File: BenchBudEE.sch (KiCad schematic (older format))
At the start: 0 parts

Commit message: Module 2, Unit 13 Defining Your Inputs and Outputs
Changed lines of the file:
@@
 $EndDescr
 $Sheet
-S 3200 5700 2200 1350
+S 2100 3450 1850 3650
 U 52EBE680
 F0 "Arduino" 50
 F1 "Arduino.sch" 50
+F2 "Relay+" O R 3950 6350 60
+F3 "Relay-" I R 3950 6550 60
+F4 "MOSI" O R 3950 5550 60
+F5 "MISO" I R 3950 5700 60
+F6 "SCLK" O R 3950 5850 60
+F7 "CS_N" O R 3950 6000 60
+F8 "LED_EN" O R 3950 4850 60
+F9 "LED_FREQ" O R 3950 5050 60
+F10 "FAN_EN" O R 3950 4300 60
+F11 "TACH_MEAS" I R 3950 4450 60
 $EndSheet
 $Sheet
@@
 F0 "Relay" 50
 F1 "Relay.sch" 50
+F2 "DIN+" I L 7600 6000 60
+F3 "DIN-" I L 7600 6250 60
+F4 "Relay+" I R 9450 6000 60
+F5 "Relay-" I R 9450 6200 60
 $EndSheet
 $Sheet
-S 3200 1350 1800 1150
+S 2050 1150 1800 1150
 U 52EBE800
 F0 "Power" 50
@@
 F0 "LED_Driver" 50
 F1 "LED_Driver.sch" 50
-$EndSheet
-$Sheet
-S 7550 1000 1850 1150
-U 52EBE84E
-F0 "Fan" 50
-F1 "Fan.sch" 50
+F2 "En" I L 7550 2800 60
+F3 "FREQ" I L 7550 3000 60
+F4 "String+" I R 9400 2800 60
+F5 "String-" O R 9400 3000 60
 $EndSheet
 $Sheet
@@
 F2 "TC IN +" I R 9450 4250 60
 F3 "TC IN -" I R 9450 4500 60
+F4 "MOSI" I L 7600 4250 60
+F5 "MISO" O L 7600 4400 60
+F6 "SCLK" I L 7600 4550 60
+F7 "CS_N" I L 7600 4700 60
+$EndSheet
+$Sheet
+S 7550 1000 1850 1150
+U 52EBE84E
+F0 "Fan" 50
+F1 "Fan.sch" 50
+F2 "Power+" O R 9400 1200 60
+F3 "Power-" I R 9400 1400 60
+F4 "Tach" I R 9400 1600 60
+F5 "Tack_Out" O L 7550 1600 60
+F6 "Fan_In" I L 7550 1200 60
 $EndSheet
 $EndSCHEMATC

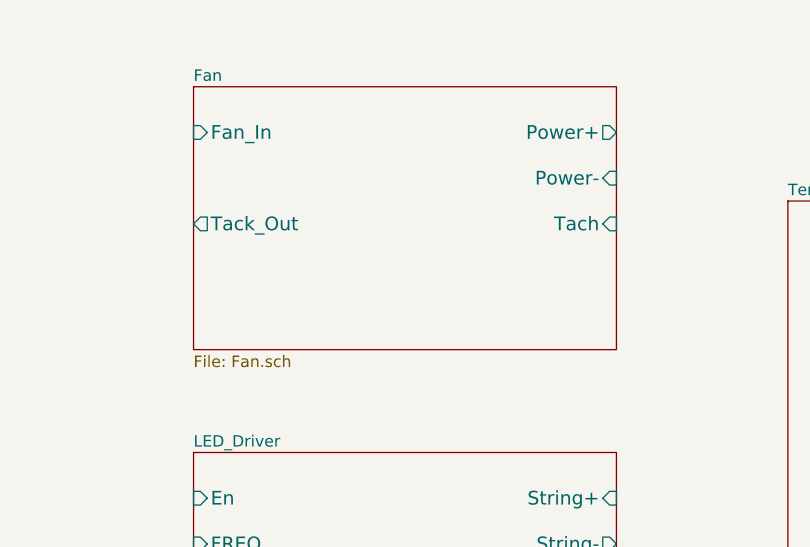
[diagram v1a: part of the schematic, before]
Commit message: 3.4 Understanding The Current/Fan Driver Module Added circuit to the Current/Fan Driver module
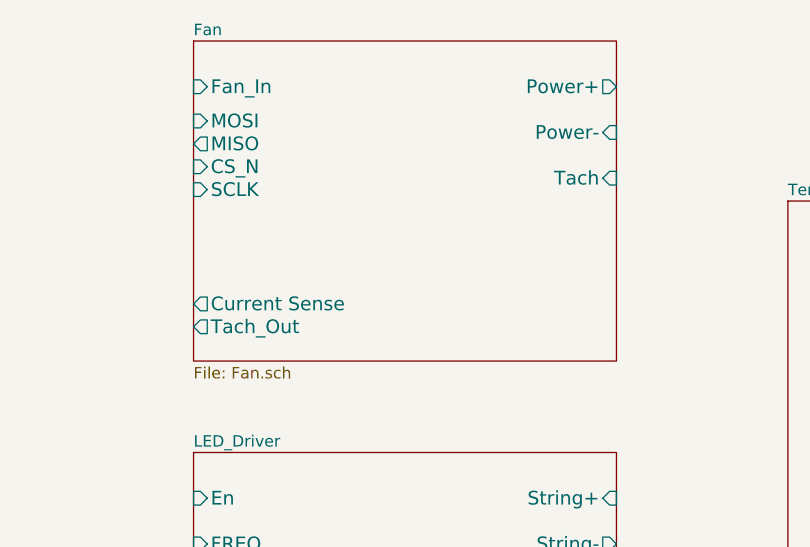
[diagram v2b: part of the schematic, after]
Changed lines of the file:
@@
 $EndSheet
 $Sheet
-S 7550 1000 1850 1150
+S 7550 800  1850 1400
 U 52EBE84E
 F0 "Fan" 50
 F1 "Fan.sch" 50
-F2 "Power+" O R 9400 1200 60
-F3 "Power-" I R 9400 1400 60
-F4 "Tach" I R 9400 1600 60
-F5 "Tack_Out" O L 7550 1600 60
-F6 "Fan_In" I L 7550 1200 60
+F2 "Power+" O R 9400 1000 60
+F3 "Power-" I R 9400 1200 60
+F4 "Tach" I R 9400 1400 60
+F5 "Tach_Out" O L 7550 2050 60
+F6 "Fan_In" I L 7550 1000 60
+F7 "Current Sense" O L 7550 1950 60
+F8 "MOSI" I L 7550 1150 60
+F9 "MISO" O L 7550 1250 60
+F10 "CS_N" I L 7550 1350 60
+F11 "SCLK" I L 7550 1450 60
 $EndSheet
 $EndSCHEMATC

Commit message: 3.5   Understanding The Relay Module
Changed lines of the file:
@@
 LIBS:valves
 LIBS:BenchBudEE-cache
-EELAYER 24 0
+EELAYER 27 0
 EELAYER END
 $Descr A4 11693 8268
@@
 Sheet 1 8
 Title ""
-Date ""
+Date "6 feb 2014"
 Rev ""
 Comp ""
@@
 F0 "Relay" 50
 F1 "Relay.sch" 50
-F2 "DIN+" I L 7600 6000 60
-F3 "DIN-" I L 7600 6250 60
-F4 "Relay+" I R 9450 6000 60
-F5 "Relay-" I R 9450 6200 60
+F2 "NC" B R 9450 6600 60
+F3 "NO" B R 9450 6700 60
+F4 "COM" B R 9450 6500 60
+F5 "DIN+" I L 7600 6000 60
+F6 "DIN-" I L 7600 6100 60
 $EndSheet
 $Sheet
